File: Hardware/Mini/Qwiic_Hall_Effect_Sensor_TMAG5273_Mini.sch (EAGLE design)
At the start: 7 parts, among them J1 QWIIC_RIGHT_ANGLE, J2 QWIIC_RIGHT_ANGLE, U1 TMAG5273

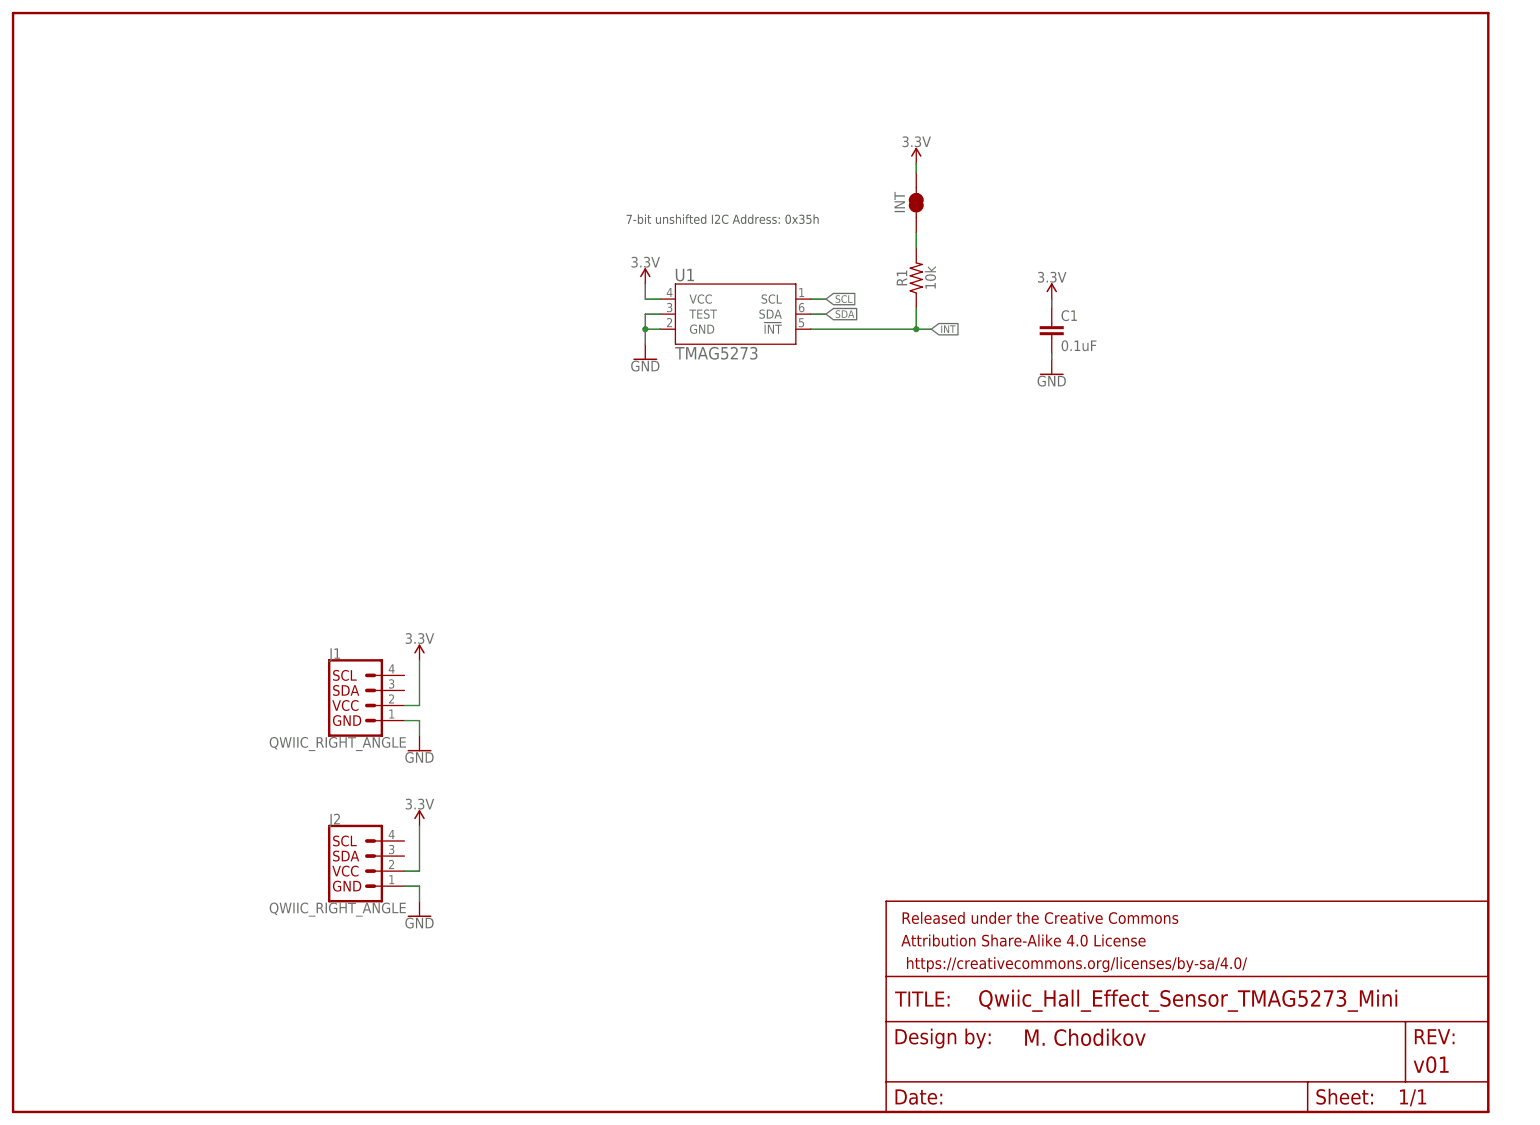
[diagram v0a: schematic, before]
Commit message: Completed schematic and routing
Need to finish aesthetics and dimensions to layout. Almost ready for review.
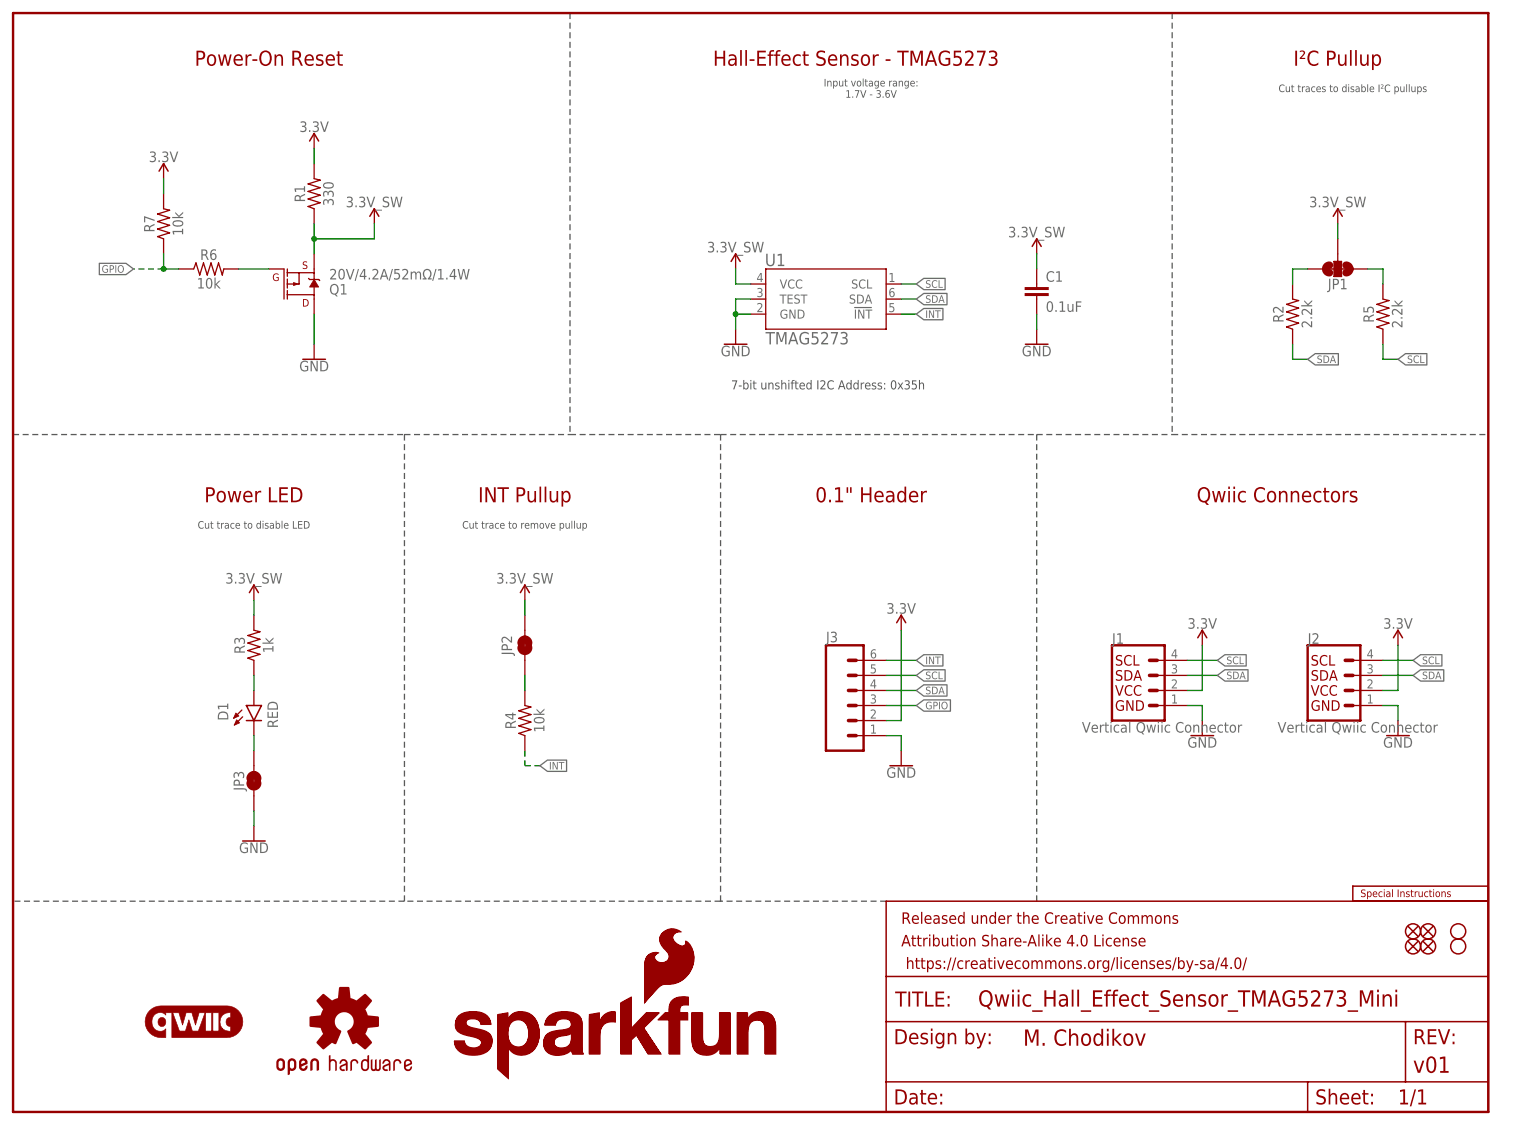
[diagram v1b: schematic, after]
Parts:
- removed INT: JUMPER-SMT_2_NC_TRACE_SILK, SparkFun-Jumpers:JUMPER-SMT_2_NC_TRACE_SILK
- added D1: RED, SparkFun-LED:LED-RED0603
- added FD1, FD2, FD3, FD4: FIDUCIAL1X2, SparkFun-Aesthetics:FIDUCIAL1X2
- added H2, H4: STAND-OFF, SparkFun-Hardware:STAND-OFF
- added J3: (no value), SparkFun-Connectors:CONN_06NO_SILK_FEMALE_PTH
- added JP1: JUMPER-SMT_3_2-NC_TRACE_SILK, SparkFun-Jumpers:JUMPER-SMT_3_2-NC_TRACE_SILK
- added JP2, JP3: JUMPER-SMT_2_NC_TRACE_SILK, SparkFun-Jumpers:JUMPER-SMT_2_NC_TRACE_SILK
- added LOGO1: OSHW-LOGOMINI, SparkFun-Aesthetics:OSHW-LOGOMINI
- added LOGO2: SFE_LOGO_NAME_FLAME5_MM, SparkFun-Aesthetics:SFE_LOGO_NAME_FLAME5_MM
- added LOGO3: QWIIC_LOGO_4MM, SparkFun-Aesthetics:QWIIC_LOGO_4MM
- added LOGO4: SFE_LOGO_NAME7_MM, SparkFun-Aesthetics:SFE_LOGO_NAME7_MM
- added LOGO5: SPECIAL_INSTRUCTIONS-ORDERING, SparkFun-Aesthetics:SPECIAL_INSTRUCTIONS-ORDERING
- added LOGO6: SFE_LOGO_FLAME0.05_INCH, SparkFun-Aesthetics:SFE_LOGO_FLAME0.05_INCH
- added Q1: 20V/4.2A/52mΩ/1.4W, SparkFun-DiscreteSemi:MOSFET_PCH-DMG2305UX-7
- added R2, R5: 2.2k, SparkFun-Resistors:2.2KOHM-0603-1/10W-1%
- added R3: 1k, SparkFun-Resistors:1KOHM-0603-1/10W-1%
- added R4, R6, R7: 10k, SparkFun-Resistors:10KOHM-0603-1/10W-1%
- C1: device SparkFun-Capacitors:0.1UF-0402-10V-10%-X7R -> SparkFun-Capacitors:0.1UF-0603-25V-10%-X7R-WE
- J1, J2: value QWIIC_RIGHT_ANGLE -> Vertical Qwiic Connector; device SparkFun-Connectors:QWIIC_CONNECTORJS-1MM -> SparkFun-Connectors:QWIIC_CONNECTOR
- R1: value 10k -> 330; device SparkFun-Resistors:10KOHM-0603-1/10W-1% -> SparkFun-Resistors:330OHM-0603-1/10W-1%
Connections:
- removed net N$3: INT.1, R1.2
- new net 3.3V_SW: C1.1, JP1.2, JP2.2, Q1.S, R1.1, R3.2, U1.VCC
- new net GPIO: J3.3, R6.1, R7.1
- new net N$1: D1.C, JP3.2
- new net N$2: JP1.3, R2.2
- new net N$4: D1.A, R3.1
- new net N$5: JP2.1, R4.2
- new net N$6: JP1.1, R5.2
- new net N$7: Q1.G, R6.2
- net 3.3V: now also J3.2, R1.2, R7.2; no longer C1.1, INT.2, U1.VCC
- net GND: now also J3.1, JP3.1, Q1.D
- net INT: now also J3.6, R4.1; no longer R1.1
- net SCL: now also J1.4, J2.4, J3.5, R5.1
- net SDA: now also J1.3, J2.3, J3.4, R2.1
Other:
- note added: "0.1" Header"
- note added: "Cut trace to disable LED"
- note added: "Cut trace to remove pullup"
- note added: "Cut traces to disable I²C pullups"
- note added: "Hall-Effect Sensor - TMAG5273"
- note added: "INT Pullup"
- note added: "Input voltage range: 1.7V - 3.6V"
- note added: "I²C Pullup"
- note added: "Power LED"
- note added: "Power-On Reset"
- note added: "Qwiic Connectors"
- moved on the sheet: C1, J1, J2, R1, U1

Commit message: Updates for design review
Changed LED and associated resistor to have the correct part and value; added dimension lines and further notes on the layout; adjusted aesthetics in schematic to now be the same as each other (minus the change in Qwiic connectors and number of standoffs)
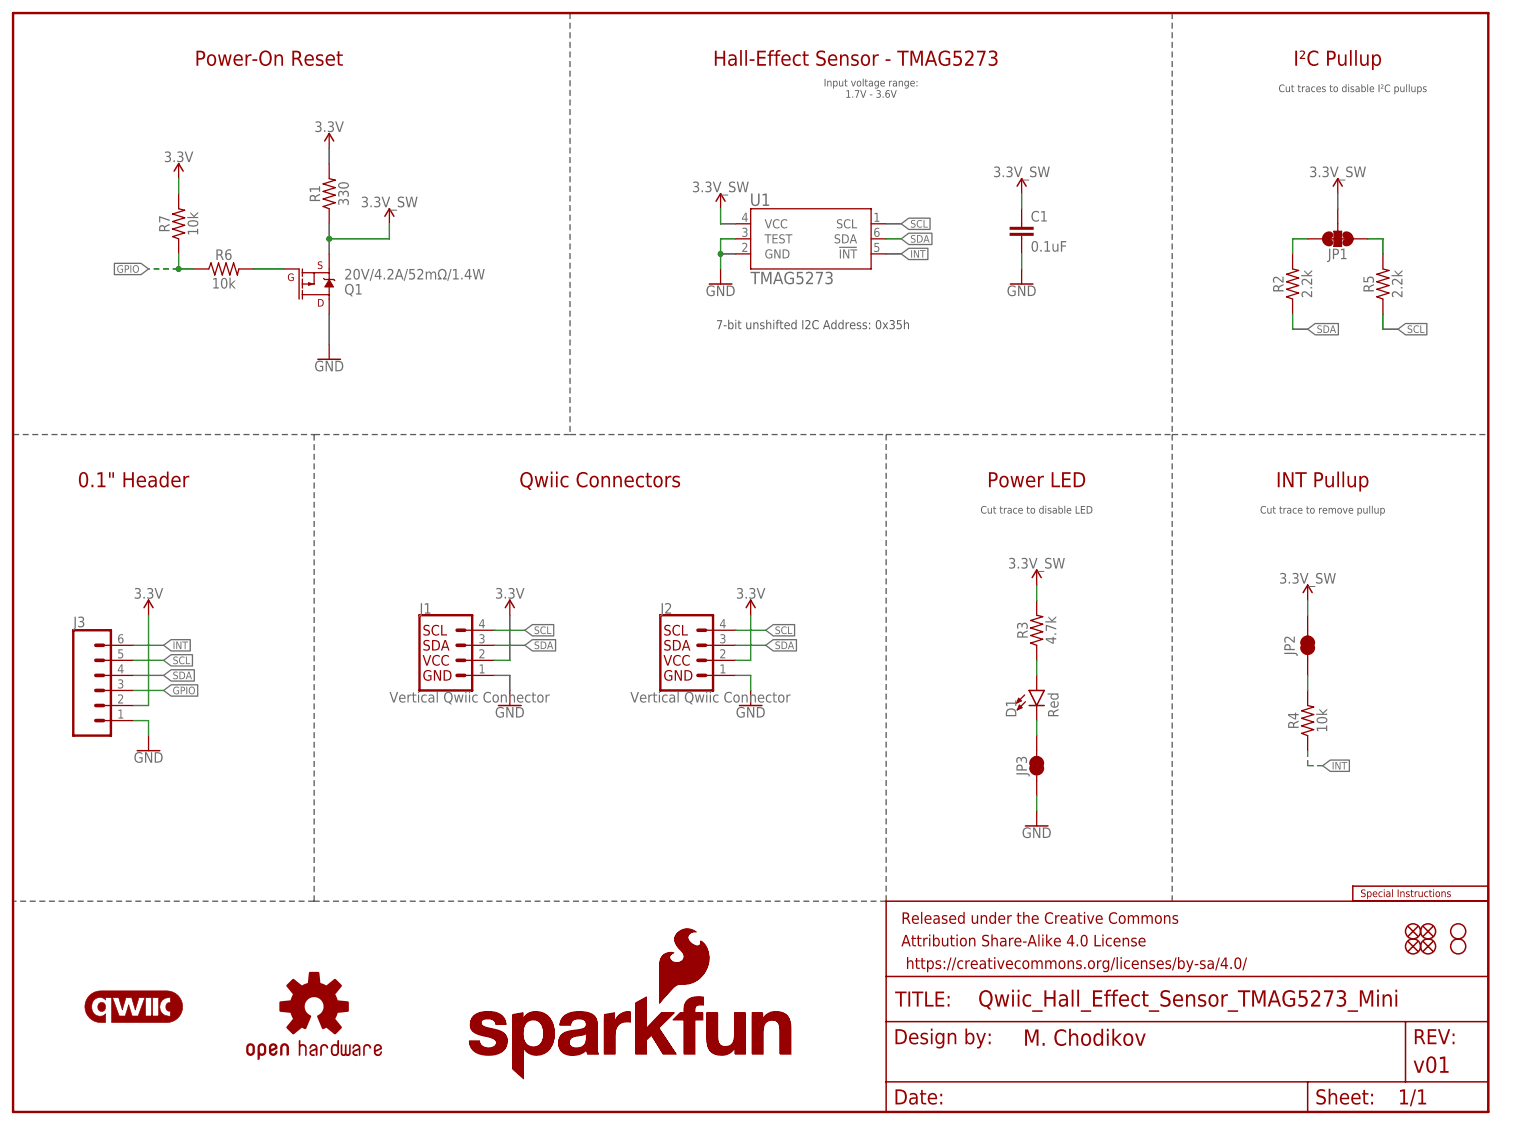
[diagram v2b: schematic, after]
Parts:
- D1: value RED -> Red; device SparkFun-LED:LED-RED0603 -> SparkFun-LED:LED-RED_0603-KB
- R3: value 1k -> 4.7k; device SparkFun-Resistors:1KOHM-0603-1/10W-1% -> SparkFun-Resistors:4.7KOHM-0603-1/10W-1%
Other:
- moved on the sheet: C1, D1, J1, J2, J3, JP1, JP2, JP3, Q1, R1, R2, R3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

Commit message: Ready for review
Updates from ENG Checklist - Small tweaks added  - updated ordering of PTH headers for SDA and SCL, fixed final errors on design
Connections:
- net GPIO: now also J3.5; no longer J3.3
- net SCL: now also J3.4; no longer J3.5
- net SDA: now also J3.3; no longer J3.4
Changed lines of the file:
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@@
 <grid distance="0.1" unitdist="inch" unit="inch" style="lines" multiple="1" display="no" altdistance="0.01" altunitdist="inch" altunit="inch"/>
 <layers>
-<layer number="1" name="Top" color="4" fill="1" visible="yes" active="no"/>
-<layer number="2" name="Route2" color="16" fill="1" visible="yes" active="no"/>
-<layer number="15" name="Route15" color="23" fill="1" visible="yes" active="no"/>
-<layer number="16" name="Bottom" color="1" fill="1" visible="yes" active="no"/>
-<layer number="17" name="Pads" color="2" fill="1" visible="yes" active="no"/>
-<layer number="18" name="Vias" color="2" fill="1" visible="yes" active="no"/>
-<layer number="19" name="Unrouted" color="6" fill="1" visible="yes" active="no"/>
-<layer number="20" name="Dimension" color="24" fill="1" visible="yes" active="no"/>
-<layer number="21" name="tPlace" color="16" fill="1" visible="yes" active="no"/>
-<layer number="22" name="bPlace" color="14" fill="1" visible="yes" active="no"/>
-<layer number="23" name="tOrigins" color="15" fill="1" visible="yes" active="no"/>
-<layer number="24" name="bOrigins" color="15" fill="1" visible="yes" active="no"/>
-<layer number="25" name="tNames" color="7" fill="1" visible="yes" active="no"/>
-<layer number="26" name="bNames" color="7" fill="1" visible="yes" active="no"/>
-<layer number="27" name="tValues" color="7" fill="1" visible="yes" active="no"/>
-<layer number="28" name="bValues" color="7" fill="1" visible="yes" active="no"/>
+<layer number="1" name="Top" color="4" fill="1" visible="no" active="no"/>
+<layer number="2" name="Route2" color="16" fill="1" visible="no" active="no"/>
+<layer number="15" name="Route15" color="23" fill="1" visible="no" active="no"/>
+<layer number="16" name="Bottom" color="1" fill="1" visible="no" active="no"/>
+<layer number="17" name="Pads" color="2" fill="1" visible="no" active="no"/>
+<layer number="18" name="Vias" color="2" fill="1" visible="no" active="no"/>
+<layer number="19" name="Unrouted" color="6" fill="1" visible="no" active="no"/>
+<layer number="20" name="Dimension" color="24" fill="1" visible="no" active="no"/>
+<layer number="21" name="tPlace" color="16" fill="1" visible="no" active="no"/>
+<layer number="22" name="bPlace" color="14" fill="1" visible="no" active="no"/>
+<layer number="23" name="tOrigins" color="15" fill="1" visible="no" active="no"/>
+<layer number="24" name="bOrigins" color="15" fill="1" visible="no" active="no"/>
+<layer number="25" name="tNames" color="7" fill="1" visible="no" active="no"/>
+<layer number="26" name="bNames" color="7" fill="1" visible="no" active="no"/>
+<layer number="27" name="tValues" color="7" fill="1" visible="no" active="no"/>
+<layer number="28" name="bValues" color="7" fill="1" visible="no" active="no"/>
 <layer number="29" name="tStop" color="7" fill="3" visible="no" active="no"/>
 <layer number="30" name="bStop" color="7" fill="6" visible="no" active="no"/>
@@
 <layer number="35" name="tGlue" color="7" fill="4" visible="no" active="no"/>
 <layer number="36" name="bGlue" color="7" fill="5" visible="no" active="no"/>
-<layer number="37" name="tTest" color="7" fill="1" visible="yes" active="no"/>
-<layer number="38" name="bTest" color="7" fill="1" visible="yes" active="no"/>
+<layer number="37" name="tTest" color="7" fill="1" visible="no" active="no"/>
+<layer number="38" name="bTest" color="7" fill="1" visible="no" active="no"/>
 <layer number="39" name="tKeepout" color="4" fill="11" visible="no" active="no"/>
 <layer number="40" name="bKeepout" color="1" fill="11" visible="no" active="no"/>
@@
 <layer number="44" name="Drills" color="7" fill="1" visible="no" active="no"/>
 <layer number="45" name="Holes" color="7" fill="1" visible="no" active="no"/>
-<layer number="46" name="Milling" color="3" fill="1" visible="yes" active="no"/>
-<layer number="47" name="Measures" color="7" fill="1" visible="yes" active="no"/>
-<layer number="48" name="Document" color="7" fill="1" visible="yes" active="no"/>
-<layer number="49" name="Reference" color="7" fill="1" visible="yes" active="no"/>
-<layer number="50" name="dxf" color="7" fill="1" visible="yes" active="no"/>
-<layer number="51" name="tDocu" color="6" fill="1" visible="yes" active="no"/>
-<layer number="52" name="bDocu" color="7" fill="1" visible="yes" active="no"/>
-<layer number="53" name="tGND_GNDA" color="7" fill="9" visible="yes" active="no"/>
-<layer number="54" name="bGND_GNDA" color="1" fill="9" visible="yes" active="no"/>
-<layer number="56" name="wert" color="7" fill="1" visible="yes" active="no"/>
-<layer number="57" name="tCAD" color="7" fill="1" visible="yes" active="no"/>
-<layer number="58" name="bCAD" color="7" fill="1" visible="yes" active="no"/>
-<layer number="59" name="tCarbon" color="7" fill="1" visible="yes" active="no"/>
-<layer number="60" name="bCarbon" color="7" fill="1" visible="yes" active="no"/>
+<layer number="46" name="Milling" color="3" fill="1" visible="no" active="no"/>
+<layer number="47" name="Measures" color="7" fill="1" visible="no" active="no"/>
+<layer number="48" name="Document" color="7" fill="1" visible="no" active="no"/>
+<layer number="49" name="Reference" color="7" fill="1" visible="no" active="no"/>
+<layer number="50" name="dxf" color="7" fill="1" visible="no" active="no"/>
+<layer number="51" name="tDocu" color="6" fill="1" visible="no" active="no"/>
+<layer number="52" name="bDocu" color="7" fill="1" visible="no" active="no"/>
+<layer number="53" name="tGND_GNDA" color="7" fill="9" visible="no" active="no"/>
+<layer number="54" name="bGND_GNDA" color="1" fill="9" visible="no" active="no"/>
+<layer number="56" name="wert" color="7" fill="1" visible="no" active="no"/>
+<layer number="57" name="tCAD" color="7" fill="1" visible="no" active="no"/>
+<layer number="58" name="bCAD" color="7" fill="1" visible="no" active="no"/>
+<layer number="59" name="tCarbon" color="7" fill="1" visible="no" active="no"/>
+<layer number="60" name="bCarbon" color="7" fill="1" visible="no" active="no"/>
 <layer number="88" name="SimResults" color="9" fill="1" visible="yes" active="yes"/>
 <layer number="89" name="SimProbes" color="9" fill="1" visible="yes" active="yes"/>
@@
 </segment>
 <segment>
-<wire x1="20.32" y1="76.2" x2="25.4" y2="76.2" width="0.1524" layer="91"/>
-<label x="25.4" y="76.2" size="1.27" layer="95" font="vector" xref="yes"/>
-<pinref part="J3" gate="J1" pin="5"/>
-</segment>
-<segment>
 <pinref part="R5" gate="G$1" pin="1"/>
 <wire x1="231.14" y1="134.62" x2="231.14" y2="132.08" width="0.1524" layer="91"/>
@@
 <label x="86.36" y="81.28" size="1.27" layer="95" font="vector" xref="yes"/>
 </segment>
+<segment>
+<wire x1="20.32" y1="73.66" x2="25.4" y2="73.66" width="0.1524" layer="91"/>
+<label x="25.4" y="73.66" size="1.27" layer="95" font="vector" xref="yes"/>
+<pinref part="J3" gate="J1" pin="4"/>
+</segment>
 </net>
 <net name="SDA" class="0">
@@
 <wire x1="149.86" y1="147.32" x2="147.32" y2="147.32" width="0.1524" layer="91"/>
 <label x="149.86" y="147.32" size="1.27" layer="95" font="vector" xref="yes"/>
-</segment>
-<segment>
-<wire x1="20.32" y1="73.66" x2="25.4" y2="73.66" width="0.1524" layer="91"/>
-<label x="25.4" y="73.66" size="1.27" layer="95" font="vector" xref="yes"/>
-<pinref part="J3" gate="J1" pin="4"/>
 </segment>
 <segment>
@@
 <wire x1="121.92" y1="78.74" x2="127" y2="78.74" width="0.1524" layer="91"/>
 <label x="127" y="78.74" size="1.27" layer="95" font="vector" xref="yes"/>
+</segment>
+<segment>
+<wire x1="20.32" y1="71.12" x2="25.4" y2="71.12" width="0.1524" layer="91"/>
+<label x="25.4" y="71.12" size="1.27" layer="95" font="vector" xref="yes"/>
+<pinref part="J3" gate="J1" pin="3"/>
 </segment>
 </net>
@@
 </segment>
 <segment>
-<pinref part="J3" gate="J1" pin="3"/>
-<wire x1="20.32" y1="71.12" x2="25.4" y2="71.12" width="0.1524" layer="91"/>
-<label x="25.4" y="71.12" size="1.27" layer="95" font="vector" xref="yes"/>
-</segment>
-</net>
+<wire x1="20.32" y1="76.2" x2="25.4" y2="76.2" width="0.1524" layer="91"/>
+<label x="25.4" y="76.2" size="1.27" layer="95" font="vector" xref="yes"/>
+<pinref part="J3" gate="J1" pin="5"/>
+</segment>
+</net>
